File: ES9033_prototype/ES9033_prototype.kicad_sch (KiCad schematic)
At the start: 8 parts, among them J101 Conn_01x02, J102 Conn_01x04, J103 Conn_01x04, J104 Conn_01x04

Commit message: added schematic title
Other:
- company: (none) -> Fabian Muehlberger 
- title: (none) -> ES9033 DAC prototype
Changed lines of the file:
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@@
 (kicad_sch (version 20211123) (generator eeschema)
   (paper "A4")
+  (title_block
+    (title "ES9033 DAC prototype")
+    (date "2022-09-09")
+    (rev "0.1")
+    (company "Fabian Muehlberger ")
+  )
   (junction (at 262.89 149.86) (diameter 0) (color 0 0 0 0)
   )

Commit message: changed header
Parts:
- removed J102, J103: Conn_01x04, Connector_PinHeader_2.54mm:PinHeader_1x04_P2.54mm_Vertical, symbol Connector_Generic:Conn_01x04
- added J1, J2: Conn_02x04_Counter_Clockwise, Connector_PinHeader_2.54mm:PinHeader_2x04_P2.54mm_Vertical, symbol Connector_Generic:Conn_02x04_Counter_Clockwise
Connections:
- net DAC_ES9033/ADDR0: now also J1.3 (Pin_3)
- net DAC_ES9033/ADDR1: now also J1.4 (Pin_4)
- net DAC_ES9033/DAC_BCK: now also J2.2 (Pin_2)
- net DAC_ES9033/DAC_SDO: now also J2.4 (Pin_4)
- net DAC_ES9033/DAC_WS: now also J2.3 (Pin_3)
- net DAC_ES9033/SCL: now also J1.2 (Pin_2)
- net DAC_ES9033/SDA: now also J1.1 (Pin_1)
- net GND: now also J1.5 (Pin_5), J1.6 (Pin_6), J1.7 (Pin_7), J1.8 (Pin_8), J2.5 (Pin_5), J2.6 (Pin_6), J2.7 (Pin_7), J2.8 (Pin_8)
- new net DAC_ES9033/MCLK: J2.1 (Pin_1)
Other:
- sheet DAC_ES9033 ports: added MCLK; removed DAC_MCLK
- moved on the sheet: J101, J104

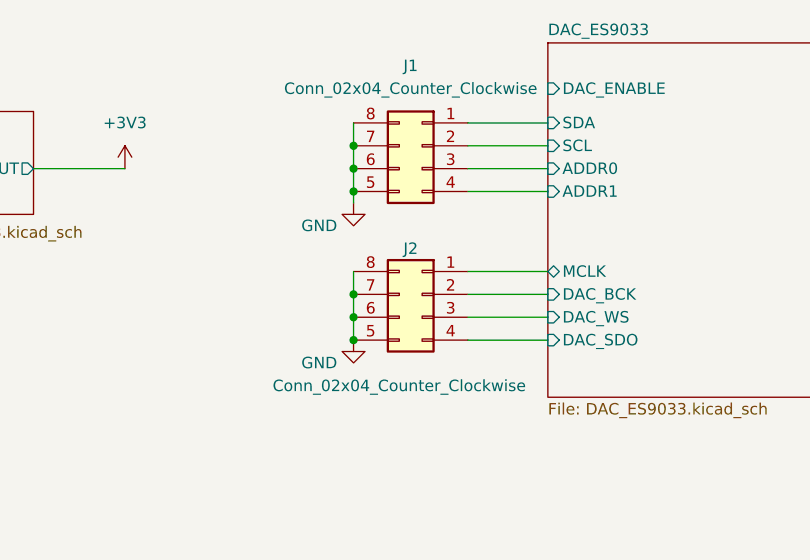
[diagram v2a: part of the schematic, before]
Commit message: changed header placement
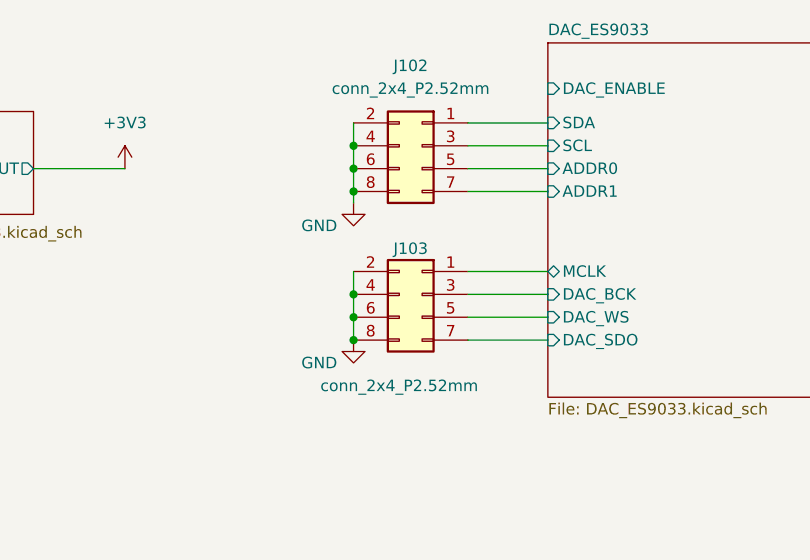
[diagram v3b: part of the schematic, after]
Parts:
- J102: renamed from J1; value Conn_02x04_Counter_Clockwise -> conn_2x4_P2.52mm; symbol Connector_Generic:Conn_02x04_Counter_Clockwise -> Connector_Generic:Conn_02x04_Odd_Even
- J103: renamed from J2; value Conn_02x04_Counter_Clockwise -> conn_2x4_P2.52mm; symbol Connector_Generic:Conn_02x04_Counter_Clockwise -> Connector_Generic:Conn_02x04_Odd_Even
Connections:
- net DAC_ES9033/ADDR0: now also J102.5 (Pin_5); no longer J102.3 (Pin_3)
- net DAC_ES9033/ADDR1: now also J102.7 (Pin_7); no longer J102.4 (Pin_4)
- net DAC_ES9033/DAC_BCK: now also J103.3 (Pin_3); no longer J103.2 (Pin_2)
- net DAC_ES9033/DAC_SDO: now also J103.7 (Pin_7); no longer J103.4 (Pin_4)
- net DAC_ES9033/DAC_WS: now also J103.5 (Pin_5); no longer J103.3 (Pin_3)
- net DAC_ES9033/SCL: now also J102.3 (Pin_3); no longer J102.2 (Pin_2)
- net GND: now also J102.2 (Pin_2), J102.4 (Pin_4), J103.2 (Pin_2), J103.4 (Pin_4); no longer J102.5 (Pin_5), J102.7 (Pin_7), J103.5 (Pin_5), J103.7 (Pin_7)
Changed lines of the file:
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@@
   (symbol (lib_id "power:GND") (at 124.46 97.79 0) (unit 1)
     (in_bom yes) (on_board yes)
-    (property "Reference" "#PWR02" (id 0) (at 124.46 104.14 0)
+    (property "Reference" "#PWR0105" (id 0) (at 124.46 104.14 0)
       (effects (font (size 1.27 1.27)) hide)
     )
@@
   (symbol (lib_id "power:GND") (at 124.46 82.55 0) (unit 1)
     (in_bom yes) (on_board yes)
-    (property "Reference" "#PWR01" (id 0) (at 124.46 88.9 0)
+    (property "Reference" "#PWR0104" (id 0) (at 124.46 88.9 0)
       (effects (font (size 1.27 1.27)) hide)
     )
@@
     (pin "1")
   )
-  (symbol (lib_id "Connector_Generic:Conn_02x04_Counter_Clockwise") (at 132.08 76.2 0) (mirror y) (unit 1)
-    (in_bom yes) (on_board yes) (fields_autoplaced)
-    (property "Reference" "J1" (id 0) (at 130.81 67.31 0))
-    (property "Value" "Conn_02x04_Counter_Clockwise" (id 1) (at 130.81 69.85 0))
+  (symbol (lib_id "Connector_Generic:Conn_02x04_Odd_Even") (at 132.08 76.2 0) (mirror y) (unit 1)
+    (in_bom yes) (on_board yes) (fields_autoplaced)
+    (property "Reference" "J102" (id 0) (at 130.81 67.31 0))
+    (property "Value" "conn_2x4_P2.52mm" (id 1) (at 130.81 69.85 0))
     (property "Footprint" "Connector_PinHeader_2.54mm:PinHeader_2x04_P2.54mm_Vertical" (id 2) (at 132.08 76.2 0)
       (effects (font (size 1.27 1.27)) hide)
@@
     (pin "1")
   )
-  (symbol (lib_id "Connector_Generic:Conn_02x04_Counter_Clockwise") (at 132.08 92.71 0) (mirror y) (unit 1)
-    (in_bom yes) (on_board yes)
-    (property "Reference" "J2" (id 0) (at 130.81 87.63 0))
-    (property "Value" "Conn_02x04_Counter_Clockwise" (id 1) (at 129.54 102.87 0))
+  (symbol (lib_id "Connector_Generic:Conn_02x04_Odd_Even") (at 132.08 92.71 0) (mirror y) (unit 1)
+    (in_bom yes) (on_board yes)
+    (property "Reference" "J103" (id 0) (at 130.81 87.63 0))
+    (property "Value" "conn_2x4_P2.52mm" (id 1) (at 129.54 102.87 0))
     (property "Footprint" "Connector_PinHeader_2.54mm:PinHeader_2x04_P2.54mm_Vertical" (id 2) (at 132.08 92.71 0)
       (effects (font (size 1.27 1.27)) hide)
@@
   (symbol (lib_id "power:GND") (at 266.7 149.86 0) (unit 1)
     (in_bom yes) (on_board yes) (fields_autoplaced)
-    (property "Reference" "#PWR0104" (id 0) (at 266.7 156.21 0)
+    (property "Reference" "#PWR0106" (id 0) (at 266.7 156.21 0)
       (effects (font (size 1.27 1.27)) hide)
     )
@@
       (reference "#FLG0203") (unit 1) (value "PWR_FLAG") (footprint "")
     )
-    (path "/4e8ca946-9d9b-439e-bc95-c24b071db66f"
-      (reference "#PWR01") (unit 1) (value "GND") (footprint "")
-    )
-    (path "/00fdaa9b-d752-4c3a-818e-fa033bbf760b"
-      (reference "#PWR02") (unit 1) (value "GND") (footprint "")
-    )
     (path "/0142f273-de18-401b-b08d-d89c05334fd3"
       (reference "#PWR0101") (unit 1) (value "+5V") (footprint "")
@@
       (reference "#PWR0103") (unit 1) (value "+3V3") (footprint "")
     )
+    (path "/4e8ca946-9d9b-439e-bc95-c24b071db66f"
+      (reference "#PWR0104") (unit 1) (value "GND") (footprint "")
+    )
+    (path "/00fdaa9b-d752-4c3a-818e-fa033bbf760b"
+      (reference "#PWR0105") (unit 1) (value "GND") (footprint "")
+    )
     (path "/decf0f3b-92e5-40fb-b7f9-88a667933c33"
-      (reference "#PWR0104") (unit 1) (value "GND") (footprint "")
+      (reference "#PWR0106") (unit 1) (value "GND") (footprint "")
     )
     (path "/c8046807-9378-4c94-8ff5-7d9c7828f19d/2aa20c33-c182-4bb0-a5d2-9e34378be50a"
@@
       (reference "H104") (unit 1) (value "MountingHole_Pad") (footprint "MountingHole:MountingHole_3.2mm_M3_DIN965_Pad")
     )
-    (path "/9b06b510-93d4-45d5-a04b-3b1b5bbebedf"
-      (reference "J1") (unit 1) (value "Conn_02x04_Counter_Clockwise") (footprint "Connector_PinHeader_2.54mm:PinHeader_2x04_P2.54mm_Vertical")
-    )
-    (path "/d2f20dd3-27db-439d-8c83-bfefe885cc0f"
-      (reference "J2") (unit 1) (value "Conn_02x04_Counter_Clockwise") (footprint "Connector_PinHeader_2.54mm:PinHeader_2x04_P2.54mm_Vertical")
-    )
-    (path "/c8046807-9378-4c94-8ff5-7d9c7828f19d/9023a2fa-8091-414c-b234-f3c004b16169"
-      (reference "J3") (unit 1) (value "Conn_02x02_Counter_Clockwise") (footprint "Connector_PinHeader_2.54mm:PinHeader_2x02_P2.54mm_Vertical")
-    )
     (path "/90fd9dde-74d2-4938-a42f-3dbde0fa6171"
       (reference "J101") (unit 1) (value "Conn_01x02") (footprint "Connector_PinHeader_2.54mm:PinHeader_1x02_P2.54mm_Vertical")
     )
+    (path "/9b06b510-93d4-45d5-a04b-3b1b5bbebedf"
+      (reference "J102") (unit 1) (value "conn_2x4_P2.52mm") (footprint "Connector_PinHeader_2.54mm:PinHeader_2x04_P2.54mm_Vertical")
+    )
+    (path "/d2f20dd3-27db-439d-8c83-bfefe885cc0f"
+      (reference "J103") (unit 1) (value "conn_2x4_P2.52mm") (footprint "Connector_PinHeader_2.54mm:PinHeader_2x04_P2.54mm_Vertical")
+    )
     (path "/3cbca4d3-def2-408b-a89a-fad302128d48"
       (reference "J104") (unit 1) (value "Conn_01x04") (footprint "Connector_PinHeader_2.54mm:PinHeader_1x04_P2.54mm_Vertical")
     )
+    (path "/c8046807-9378-4c94-8ff5-7d9c7828f19d/263d11db-7063-4f55-a5e5-b3058ad42a2f"
+      (reference "JP201") (unit 1) (value "jumper_open") (footprint "Jumper:SolderJumper-2_P1.3mm_Open_Pad1.0x1.5mm")
+    )
+    (path "/c8046807-9378-4c94-8ff5-7d9c7828f19d/ca5ee9d0-9e20-424c-8b8e-42bc4002f3d1"
+      (reference "JP202") (unit 1) (value "jumper_open") (footprint "Jumper:SolderJumper-2_P1.3mm_Open_Pad1.0x1.5mm")
+    )
     (path "/c8046807-9378-4c94-8ff5-7d9c7828f19d/5d1658d0-462b-4308-8122-710b273e4bd3"
-      (reference "JP201") (unit 1) (value "Jumper_3_Open") (footprint "Connector_PinHeader_2.54mm:PinHeader_1x03_P2.54mm_Vertical")
+      (reference "JP203") (unit 1) (value "Jumper_3_Open") (footprint "Connector_PinHeader_2.54mm:PinHeader_1x03_P2.54mm_Vertical")
     )
     (path "/c8046807-9378-4c94-8ff5-7d9c7828f19d/437e341d-03bd-4037-ae2b-bfebb3748d78"
-      (reference "JP202") (unit 1) (value "Jumper_3_Open") (footprint "Connector_PinHeader_2.54mm:PinHeader_1x03_P2.54mm_Vertical")
+      (reference "JP204") (unit 1) (value "Jumper_3_Open") (footprint "Connector_PinHeader_2.54mm:PinHeader_1x03_P2.54mm_Vertical")
     )
     (path "/c8046807-9378-4c94-8ff5-7d9c7828f19d/ef7517e1-5f05-4862-9e7c-f7ea3d1037d4"
-      (reference "JP203") (unit 1) (value "Jumper_3_Open") (footprint "Connector_PinHeader_2.54mm:PinHeader_1x03_P2.54mm_Vertical")
+      (reference "JP205") (unit 1) (value "Jumper_3_Open") (footprint "Connector_PinHeader_2.54mm:PinHeader_1x03_P2.54mm_Vertical")
     )
     (path "/c8046807-9378-4c94-8ff5-7d9c7828f19d/8059282c-3882-49dd-a324-4ffc155fe971"
-      (reference "JP204") (unit 1) (value "Jumper_3_Open") (footprint "Connector_PinHeader_2.54mm:PinHeader_1x03_P2.54mm_Vertical")
+      (reference "JP206") (unit 1) (value "Jumper_3_Open") (footprint "Connector_PinHeader_2.54mm:PinHeader_1x03_P2.54mm_Vertical")
     )
     (path "/c8046807-9378-4c94-8ff5-7d9c7828f19d/b485620c-a93b-438f-afed-b8f69c641b18"
-      (reference "JP205") (unit 1) (value "Jumper_3_Open") (footprint "Connector_PinHeader_2.54mm:PinHeader_1x03_P2.54mm_Vertical")
+      (reference "JP207") (unit 1) (value "Jumper_3_Open") (footprint "Connector_PinHeader_2.54mm:PinHeader_1x03_P2.54mm_Vertical")
     )
     (path "/c8046807-9378-4c94-8ff5-7d9c7828f19d/ab747232-8d32-47a7-ac58-ee6e2a9656da"
-      (reference "JP206") (unit 1) (value "Jumper_3_Open") (footprint "Connector_PinHeader_2.54mm:PinHeader_1x03_P2.54mm_Vertical")
+      (reference "JP208") (unit 1) (value "Jumper_3_Open") (footprint "Connector_PinHeader_2.54mm:PinHeader_1x03_P2.54mm_Vertical")
     )
     (path "/c8046807-9378-4c94-8ff5-7d9c7828f19d/9544d287-8d81-40ca-9728-db87c3ea99a3"

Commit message: stuff
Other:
- sheet LDO_LT3042_3v3 renamed POWER
- sheet POWER: file LDO_LT3042_3v3.kicad_sch -> POWER.kicad_sch
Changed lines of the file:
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@@
     (stroke (width 0.1524) (type solid) (color 0 0 0 0))
     (fill (color 0 0 0 0.0000))
-    (property "Sheet name" "LDO_LT3042_3v3" (id 0) (at 69.85 71.6784 0)
+    (property "Sheet name" "POWER" (id 0) (at 69.85 71.6784 0)
       (effects (font (size 1.27 1.27)) (justify left bottom))
     )
-    (property "Sheet file" "LDO_LT3042_3v3.kicad_sch" (id 1) (at 66.04 85.09 0)
+    (property "Sheet file" "POWER.kicad_sch" (id 1) (at 69.85 83.82 0)
       (effects (font (size 1.27 1.27)) (justify left top))
     )
@@
       (reference "#PWR0226") (unit 1) (value "GND") (footprint "")
     )
+    (path "/c8046807-9378-4c94-8ff5-7d9c7828f19d/84e531e8-da58-41a8-8285-9fa0a2b754f1"
+      (reference "#PWR0227") (unit 1) (value "+3V3") (footprint "")
+    )
+    (path "/c8046807-9378-4c94-8ff5-7d9c7828f19d/17bbd268-962f-4d8d-81cf-0c9910eeffaa"
+      (reference "#PWR0228") (unit 1) (value "GND") (footprint "")
+    )
+    (path "/8f0e9a9d-7880-4661-a6fc-61fb7d9afaf3/70d3766c-4eed-40d9-b130-8967ce28c62c"
+      (reference "#PWR0301") (unit 1) (value "GND") (footprint "")
+    )
     (path "/8f0e9a9d-7880-4661-a6fc-61fb7d9afaf3/772a847f-610a-4c87-9f2b-f302f6ae022e"
-      (reference "#PWR0301") (unit 1) (value "GND") (footprint "")
+      (reference "#PWR0302") (unit 1) (value "GND") (footprint "")
     )
     (path "/8f0e9a9d-7880-4661-a6fc-61fb7d9afaf3/2971011f-0746-4149-9d9f-615fe2abdb85"
-      (reference "#PWR0302") (unit 1) (value "GND") (footprint "")
+      (reference "#PWR0303") (unit 1) (value "GND") (footprint "")
     )
     (path "/8f0e9a9d-7880-4661-a6fc-61fb7d9afaf3/84b3b00b-ca77-434e-b060-8d145efbe474"
-      (reference "#PWR0303") (unit 1) (value "GND") (footprint "")
+      (reference "#PWR0304") (unit 1) (value "GND") (footprint "")
     )
     (path "/8f0e9a9d-7880-4661-a6fc-61fb7d9afaf3/394b6daa-c3cf-4ac5-a7b2-f964820f1786"
-      (reference "#PWR0304") (unit 1) (value "GND") (footprint "")
+      (reference "#PWR0305") (unit 1) (value "GND") (footprint "")
     )
     (path "/c8046807-9378-4c94-8ff5-7d9c7828f19d/7ad81233-f4ae-4fbe-9202-46d4ad2f0fd1"
@@
       (reference "R303") (unit 1) (value "49k9") (footprint "Resistor_SMD:R_0805_2012Metric")
     )
+    (path "/c8046807-9378-4c94-8ff5-7d9c7828f19d/7552ab7c-4818-475e-a0d1-67aef51ba6e0"
+      (reference "SW201") (unit 1) (value "SW_SP3T") (footprint "Button_Switch_SMD:SW_SP3T_PCM13")
+    )
     (path "/c8046807-9378-4c94-8ff5-7d9c7828f19d/30b0f246-580b-438c-80cf-ac0ec9c741ed"
       (reference "U201") (unit 1) (value "ES9033") (footprint "Package_DFN_QFN:QFN-28-1EP_5x5mm_P0.5mm_EP3.35x3.35mm")
     )
+    (path "/8f0e9a9d-7880-4661-a6fc-61fb7d9afaf3/23e9e319-e3dd-4183-9eee-45b66d9a3c55"
+      (reference "U301") (unit 1) (value "TVS1400DRV") (footprint "Package_SON:WSON-6-1EP_2x2mm_P0.65mm_EP1x1.6mm")
+    )
     (path "/8f0e9a9d-7880-4661-a6fc-61fb7d9afaf3/71175413-a6e1-48ab-8790-8ad587722484"
-      (reference "U301") (unit 1) (value "LT3042") (footprint "Package_DFN_QFN:DFN-10-1EP_3x3mm_P0.5mm_EP1.7x2.5mm")
+      (reference "U302") (unit 1) (value "LT3042") (footprint "Package_DFN_QFN:DFN-10-1EP_3x3mm_P0.5mm_EP1.7x2.5mm")
     )
     (path "/c8046807-9378-4c94-8ff5-7d9c7828f19d/c3feb132-8988-4ed5-b90c-09c875585849"

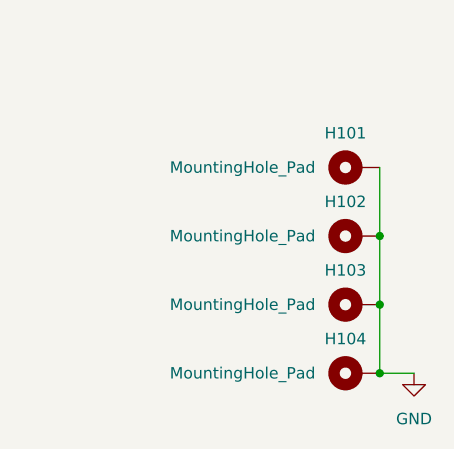
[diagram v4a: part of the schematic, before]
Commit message: removed grounding from mounting holes
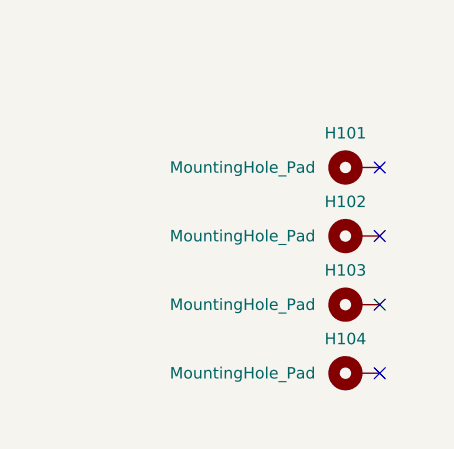
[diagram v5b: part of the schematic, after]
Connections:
- net GND: no longer H101.1, H102.1, H103.1, H104.1
- no-connect marks 0 -> 4
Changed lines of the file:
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@@
     (company "Fabian Muehlberger ")
   )
-  (junction (at 262.89 149.86) (diameter 0) (color 0 0 0 0)
-  )
   (junction (at 55.88 78.74) (diameter 0) (color 0 0 0 0)
   )
@@
   (junction (at 124.46 95.25) (diameter 0) (color 0 0 0 0)
   )
-  (junction (at 262.89 142.24) (diameter 0) (color 0 0 0 0)
-  )
-  (junction (at 262.89 134.62) (diameter 0) (color 0 0 0 0)
-  )
+  (no_connect (at 262.89 127))
+  (no_connect (at 262.89 134.62))
+  (no_connect (at 262.89 142.24))
+  (no_connect (at 262.89 149.86))
   (wire (pts (xy 190.5 76.2) (xy 196.85 76.2))
     (stroke (width 0) (type default) (color 0 0 0 0))
   )
-  (wire (pts (xy 262.89 134.62) (xy 262.89 142.24))
-    (stroke (width 0) (type default) (color 0 0 0 0))
-  )
   (wire (pts (xy 55.88 78.74) (xy 55.88 74.93))
     (stroke (width 0) (type default) (color 0 0 0 0))
@@
     (stroke (width 0) (type default) (color 0 0 0 0))
   )
-  (wire (pts (xy 262.89 142.24) (xy 262.89 149.86))
-    (stroke (width 0) (type default) (color 0 0 0 0))
-  )
   (wire (pts (xy 137.16 78.74) (xy 146.05 78.74))
     (stroke (width 0) (type default) (color 0 0 0 0))
@@
   )
   (wire (pts (xy 55.88 78.74) (xy 69.85 78.74))
-    (stroke (width 0) (type default) (color 0 0 0 0))
-  )
-  (wire (pts (xy 266.7 149.86) (xy 262.89 149.86))
-    (stroke (width 0) (type default) (color 0 0 0 0))
-  )
-  (wire (pts (xy 262.89 127) (xy 262.89 134.62))
     (stroke (width 0) (type default) (color 0 0 0 0))
   )
@@
     (pin "8")
   )
-  (symbol (lib_id "power:GND") (at 266.7 149.86 0) (unit 1)
-    (in_bom yes) (on_board yes) (fields_autoplaced)
-    (property "Reference" "#PWR0106" (id 0) (at 266.7 156.21 0)
-      (effects (font (size 1.27 1.27)) hide)
-    )
-    (property "Value" "GND" (id 1) (at 266.7 154.94 0))
-    (property "Footprint" "" (id 2) (at 266.7 149.86 0)
-      (effects (font (size 1.27 1.27)) hide)
-    )
-    (property "Datasheet" "" (id 3) (at 266.7 149.86 0)
-      (effects (font (size 1.27 1.27)) hide)
-    )
-    (pin "1")
-  )
   (sheet (at 69.85 72.39) (size 19.05 11.43)
     (stroke (width 0.1524) (type solid) (color 0 0 0 0))
@@
       (reference "#PWR0105") (unit 1) (value "GND") (footprint "")
     )
-    (path "/decf0f3b-92e5-40fb-b7f9-88a667933c33"
-      (reference "#PWR0106") (unit 1) (value "GND") (footprint "")
-    )
     (path "/c8046807-9378-4c94-8ff5-7d9c7828f19d/2aa20c33-c182-4bb0-a5d2-9e34378be50a"
